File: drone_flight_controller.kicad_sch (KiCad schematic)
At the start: 67 parts, among them J1 Conn_01x08_MountingPin, J2 USB_C_Receptacle_USB2.0_16P, U1 STM32H743VITx, U2 IST8310, U3 BMP388, U4 ICM-42688-P, U5 LT3045xDD, U6 LM5164DDA, Y1 25MHz, Y2 32.768KHz

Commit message: started placing some items
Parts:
- added H1, H2, H3, H4: MountingHole, MountingHole:MountingHole_3.2mm_M3, symbol Mechanical:MountingHole
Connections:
- net +3.3V: now also C28.1, C29.1, U2.13 (DVDD), U2.2 (AVDD)
- net IST8310_C1: now reaches C27.1, U2.10 (C1)
- net IMU_INT2: now reaches U4.9 (INT2/FSYNC/CLKIN)
- net IMU_INT renamed IMU_INT1

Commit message: more placing and routing
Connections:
- net CC1: now reaches J2.A5 (CC1), R13.1
- net CC2: now reaches J2.B5 (CC2), R12.1
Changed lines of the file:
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@@
+		)
+	)
+	(label "CC2"
+		(at 48.26 173.99 0)
+		(effects
+			(font
+				(size 1.27 1.27)
+			)
+			(justify left bottom)
 		)
 	)
@@
 		(effects
 			(font
+				(size 1.27 1.27)
+			)
+			(justify left bottom)
+		)
+	)
+	(label "CC1"
+		(at 48.26 171.45 0)
+		(effects
+			(font

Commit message: added most components
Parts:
- C17: value 82pF -> 56pF
- L1: value 56uH -> 33uH
- R3: value 64.9k -> 41.2k
- R4: value 422k -> 237k
- R5: value 220k -> 316k
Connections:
- net +3V3 is gone; now on net +3.3V: C10.1, C11.1, C12.1, C15.1, C6.1, C8.1, C9.1, FB1.2, U1.100 (VDD), U1.11 (VDD), U1.27 (VDD), U1.50 (VDD), U1.6 (VBAT), U1.75 (VDD)
- net I2C_SCL: now also U1.92 (PB6)
- net I2C_SDA: now also U1.93 (PB7)
- net BUCK_OUT renamed +5V
- net SPI_CS: no longer names the net of U1.28 (PA4)
- net SPI_CS: no longer U4.12 (AP_CS)
- new net IMU_CS: U4.12 (AP_CS)

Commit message: routing + final commit before reducing size
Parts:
- added J3: Conn_01x06_MountingPin, Connector_JST:JST_SH_BM06B-SRSS-TB_1x06-1MP_P1.00mm_Vertical, symbol Connector_Generic_MountingPin:Conn_01x06_MountingPin
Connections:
- net +5V: now also J3.1 (Pin_1)
- net GND: now also J3.2 (Pin_2), J3.MP (MountPin)
- net I2C_SCL: now also J3.6 (Pin_6)
- net I2C_SDA: now also J3.5 (Pin_5)
- new net GPS_RX: J3.3 (Pin_3)
- new net GPS_TX: J3.4 (Pin_4)

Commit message: started downsizing to 25.5mm
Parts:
- removed C19, C20: 22uF, Capacitor_SMD:C_0603_1608Metric, symbol Device:C
- H1, H2, H3, H4: footprint MountingHole:MountingHole_3.2mm_M3 -> MountingHole:MountingHole_2.2mm_M2
- J1: footprint Connector_JST:JST_SH_BM08B-SRSS-TB_1x08-1MP_P1.00mm_Vertical -> Connector_JST:JST_SH_SM08B-SRSS-TB_1x08-1MP_P1.00mm_Horizontal
- J3: footprint Connector_JST:JST_SH_BM06B-SRSS-TB_1x06-1MP_P1.00mm_Vertical -> Connector_JST:JST_SH_SM06B-SRSS-TB_1x06-1MP_P1.00mm_Horizontal
- L1: footprint Inductor_SMD:L_Bourns_SRR1210A -> Inductor_SMD:L_Vishay_IHLP-2525

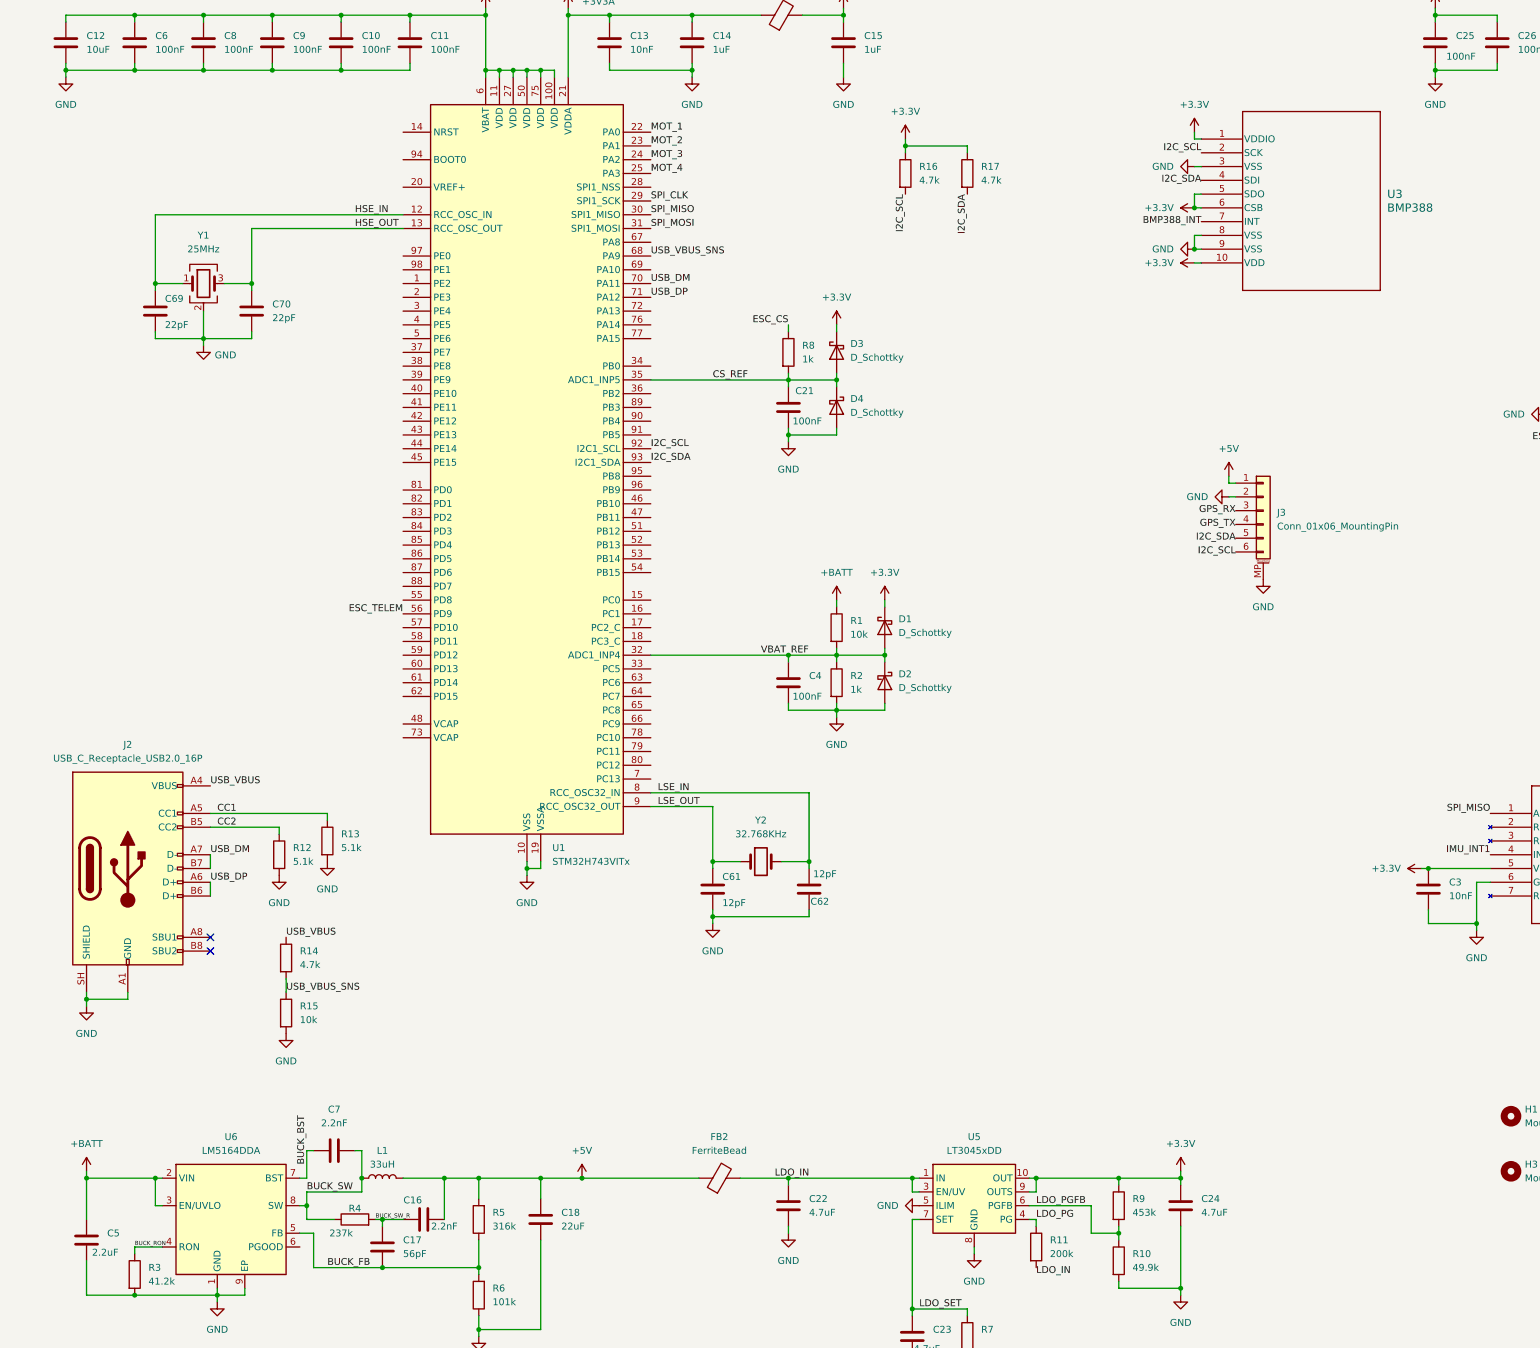
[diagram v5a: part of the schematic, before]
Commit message: added most routing, still needs to be cleaned up
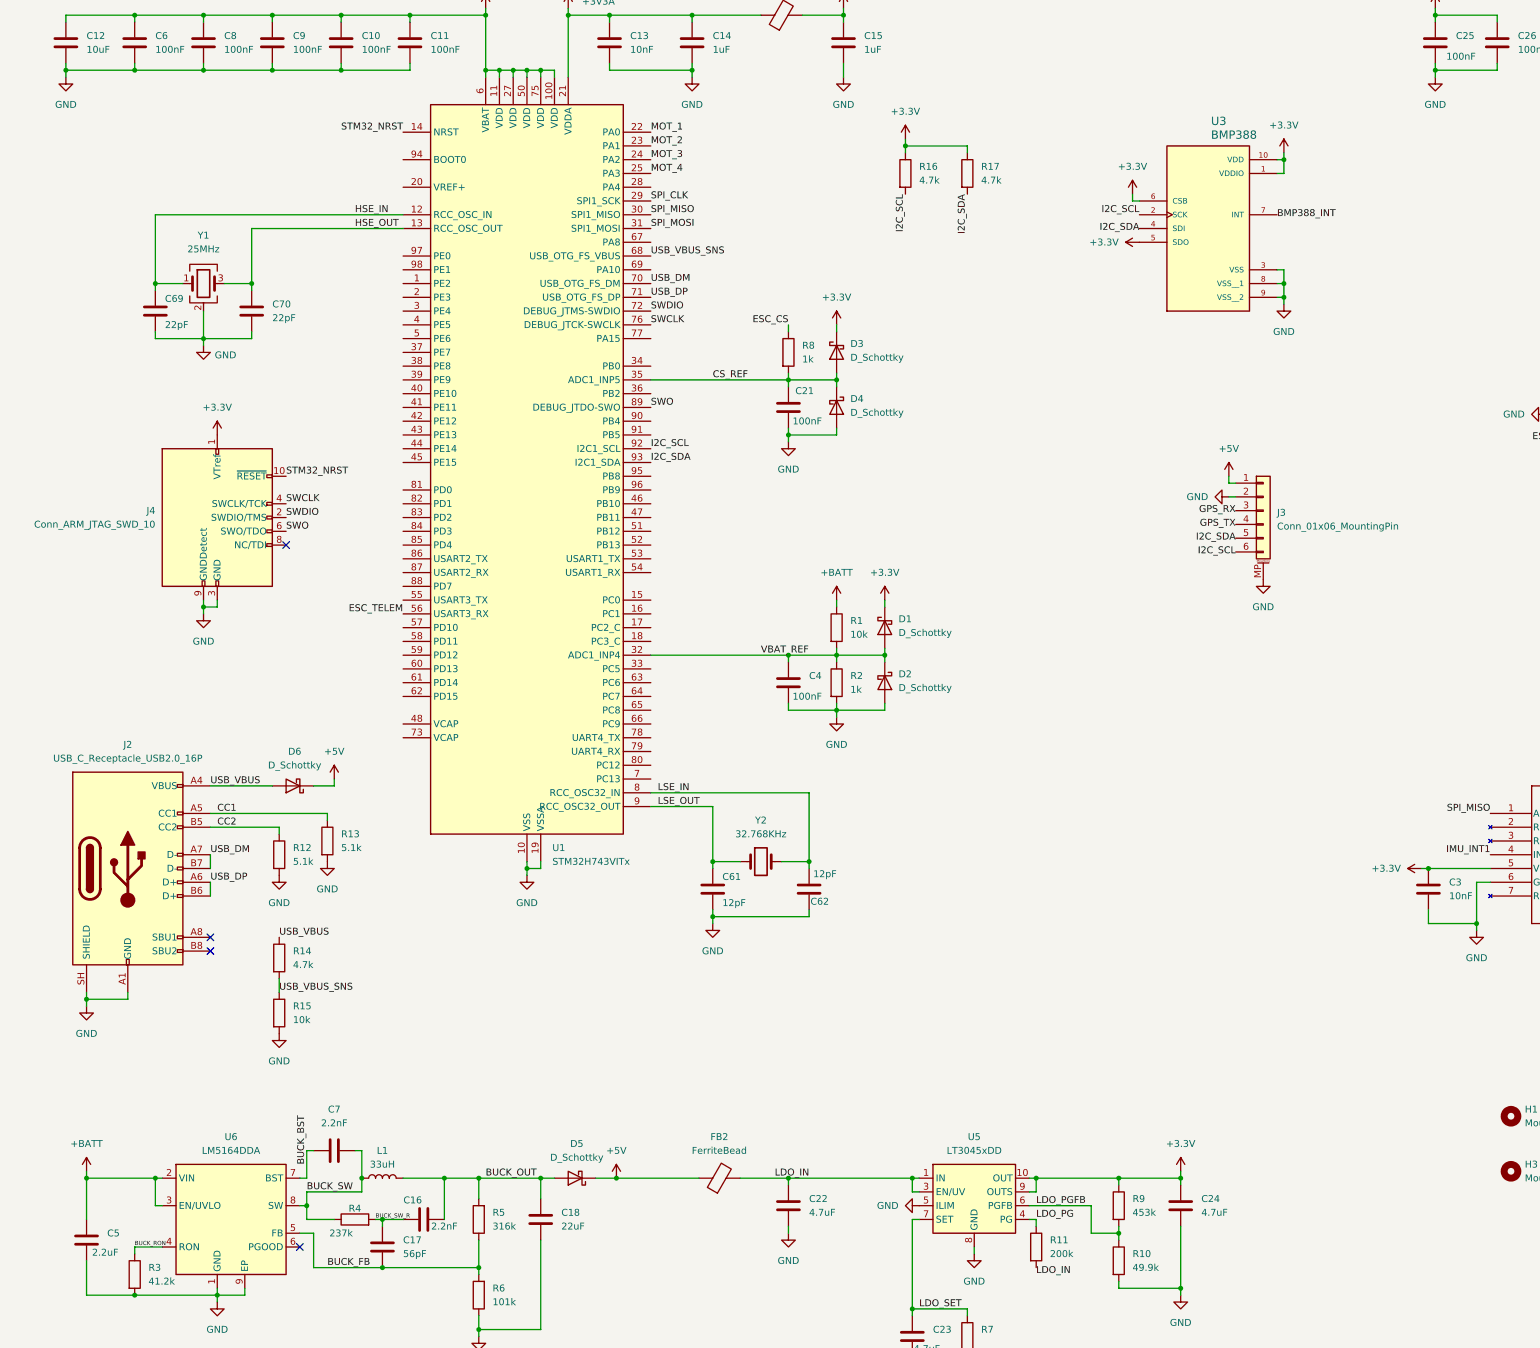
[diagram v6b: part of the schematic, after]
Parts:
- added D5, D6: D_Schottky, Diode_SMD:D_SOD-123, symbol Device:D_Schottky
- added J4: Conn_ARM_JTAG_SWD_10, Connector_PinHeader_1.27mm:PinHeader_2x05_P1.27mm_Vertical, symbol Connector:Conn_ARM_JTAG_SWD_10
- U3: footprint drone:QFN_BMP388_BOS -> drone:XDCR_BMP388; CREATOR (none) -> KARTHIK; MANUFACTURER (none) -> Bosch Sensortec; MAXIMUM_PACKAGE_HEIGHT (none) -> 0.8 mm; PARTREV (none) -> 1.7; SNAPEDA_PN (none) -> BMP388; STANDARD (none) -> Manufacturer Recommendations
- U4: footprint drone:LGA14_2P5X3X0P91_TDK -> Package_LGA:LGA-14_3x2.5mm_P0.5mm_LayoutBorder3x4y
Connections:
- net +3.3V: now also J4.1 (VTref)
- net +5V: now also D5.1 (K), D6.1 (K); no longer C16.2, C18.2, L1.2, R5.2
- net GND: now also J4.3 (GND), J4.5 (GND), J4.9 (GNDDetect)
- net USB_VBUS: now also D6.2 (A)
- net STM32_NRST: now reaches U1.14 (NRST)
- net STM32_NRST: now also J4.10 (~{RESET})
- net SWDIO: now reaches U1.72 (PA13)
- net SWDIO: now also J4.2 (SWDIO/TMS)
- net SWCLK: now reaches U1.76 (PA14)
- net SWCLK: now also J4.4 (SWCLK/TCK)
- net SWO: now reaches U1.89 (PB3)
- net SWO: now also J4.6 (SWO/TDO)
- new net BUCK_OUT: C16.2, C18.2, D5.2 (A), L1.2, R5.2
- no-connect marks 3 -> 5
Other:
- moved on the sheet: R14, R15

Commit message: removed most drc violations
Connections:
- net GPS_RX: now also U1.79 (PC11)
- net GPS_TX: now also U1.78 (PC10)
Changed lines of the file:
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@@
+		)
+	)
+	(label "GPS_TX"
+		(at 128.27 157.48 0)
+		(effects
+			(font
+				(size 1.27 1.27)
+			)
+			(justify left)
 		)
 	)
@@
 		)
 	)
+	(label "GPS_RX"
+		(at 128.27 160.02 0)
+		(effects
+			(font
+				(size 1.27 1.27)
+			)
+			(justify left)
+		)
+	)
